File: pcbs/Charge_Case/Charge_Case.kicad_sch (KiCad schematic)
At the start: 3 parts, among them J1 GSB1C41110SSHR

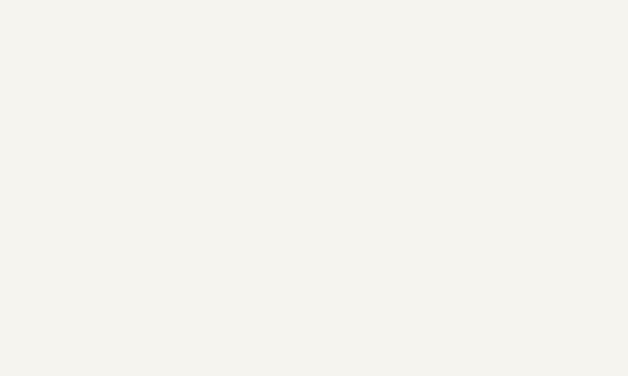
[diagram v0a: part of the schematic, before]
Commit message: update minibot fw, add pcb ordered packages
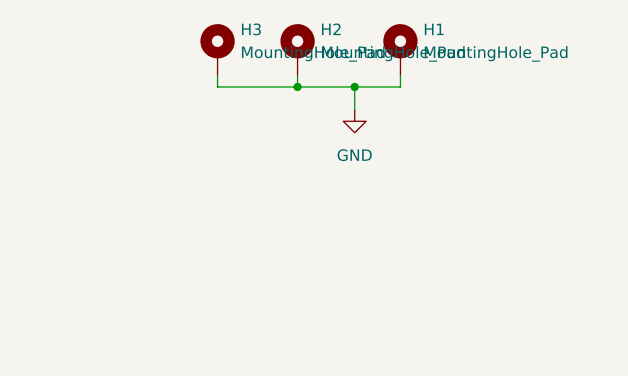
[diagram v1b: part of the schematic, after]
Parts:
- added H1, H2, H3: MountingHole_Pad, MountingHole:MountingHole_2.7mm_M2.5_DIN965_Pad_TopOnly, symbol Mechanical:MountingHole_Pad
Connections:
- net GND: now also H1.1, H2.1, H3.1
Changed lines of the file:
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@@
 (kicad_sch (version 20230121) (generator eeschema)
   (paper "A4")
+  (junction (at 242.57 35.56) (diameter 0) (color 0 0 0 0)
+  )
+  (junction (at 248.92 35.56) (diameter 0) (color 0 0 0 0)
+  )
   (no_connect (at 72.39 46.99))
   (no_connect (at 36.83 49.53))
@@
   (no_connect (at 72.39 49.53))
   (no_connect (at 72.39 54.61))
+  (wire (pts (xy 248.92 35.56) (xy 248.92 38.1))
+    (stroke (width 0) (type default))
+  )
   (wire (pts (xy 36.83 46.99) (xy 39.37 46.99))
     (stroke (width 0) (type default))
@@
     (stroke (width 0) (type default))
   )
+  (wire (pts (xy 233.68 35.56) (xy 242.57 35.56))
+    (stroke (width 0) (type default))
+  )
   (wire (pts (xy 69.85 49.53) (xy 72.39 49.53))
     (stroke (width 0) (type default))
@@
     (stroke (width 0) (type default))
   )
+  (wire (pts (xy 242.57 35.56) (xy 248.92 35.56))
+    (stroke (width 0) (type default))
+  )
+  (wire (pts (xy 242.57 34.29) (xy 242.57 35.56))
+    (stroke (width 0) (type default))
+  )
   (wire (pts (xy 31.75 36.83) (xy 39.37 36.83))
     (stroke (width 0) (type default))
@@
     (stroke (width 0) (type default))
   )
+  (wire (pts (xy 233.68 34.29) (xy 233.68 35.56))
+    (stroke (width 0) (type default))
+  )
   (wire (pts (xy 107.95 109.22) (xy 110.49 109.22))
     (stroke (width 0) (type default))
@@
     (stroke (width 0) (type default))
   )
+  (wire (pts (xy 254 35.56) (xy 248.92 35.56))
+    (stroke (width 0) (type default))
+  )
   (wire (pts (xy 36.83 44.45) (xy 36.83 46.99))
     (stroke (width 0) (type default))
@@
   )
   (wire (pts (xy 107.95 76.2) (xy 110.49 76.2))
+    (stroke (width 0) (type default))
+  )
+  (wire (pts (xy 254 34.29) (xy 254 35.56))
     (stroke (width 0) (type default))
   )
@@
   (label "CC2_SRC" (at 72.39 36.83 0) (fields_autoplaced)
     (effects (font (size 1.27 1.27)) (justify left bottom))
+  )
+  (symbol (lib_id "Mechanical:MountingHole_Pad") (at 254 31.75 0) (unit 1)
+    (in_bom yes) (on_board yes) (dnp no) (fields_autoplaced)
+    (property "Reference" "H1" (at 256.54 29.21 0)
+      (effects (font (size 1.27 1.27)) (justify left))
+    )
+    (property "Value" "MountingHole_Pad" (at 256.54 31.75 0)
+      (effects (font (size 1.27 1.27)) (justify left))
+    )
+    (property "Footprint" "MountingHole:MountingHole_2.7mm_M2.5_DIN965_Pad_TopOnly" (at 254 31.75 0)
+      (effects (font (size 1.27 1.27)) hide)
+    )
+    (property "Datasheet" "~" (at 254 31.75 0)
+      (effects (font (size 1.27 1.27)) hide)
+    )
+    (pin "1")
+    (instances
+      (project "Charge_Case"
+        (path "/c60e6ee3-9293-40aa-b626-5d3d0add00e1"
+          (reference "H1") (unit 1)
+        )
+      )
+    )
   )
   (symbol (lib_id "power:+5V") (at 31.75 52.07 90) (unit 1)
@@
     )
   )
+  (symbol (lib_id "Mechanical:MountingHole_Pad") (at 233.68 31.75 0) (unit 1)
+    (in_bom yes) (on_board yes) (dnp no) (fields_autoplaced)
+    (property "Reference" "H3" (at 236.22 29.21 0)
+      (effects (font (size 1.27 1.27)) (justify left))
+    )
+    (property "Value" "MountingHole_Pad" (at 236.22 31.75 0)
+      (effects (font (size 1.27 1.27)) (justify left))
+    )
+    (property "Footprint" "MountingHole:MountingHole_2.7mm_M2.5_DIN965_Pad_TopOnly" (at 233.68 31.75 0)
+      (effects (font (size 1.27 1.27)) hide)
+    )
+    (property "Datasheet" "~" (at 233.68 31.75 0)
+      (effects (font (size 1.27 1.27)) hide)
+    )
+    (pin "1")
+    (instances
+      (project "Charge_Case"
+        (path "/c60e6ee3-9293-40aa-b626-5d3d0add00e1"
+          (reference "H3") (unit 1)
+        )
+      )
+    )
+  )
   (symbol (lib_id "Jumper:Jumper_2_Bridged") (at 102.87 38.1 0) (unit 1)
     (in_bom yes) (on_board yes) (dnp no) (fields_autoplaced)
@@
     )
   )
+  (symbol (lib_id "Mechanical:MountingHole_Pad") (at 242.57 31.75 0) (unit 1)
+    (in_bom yes) (on_board yes) (dnp no) (fields_autoplaced)
+    (property "Reference" "H2" (at 245.11 29.21 0)
+      (effects (font (size 1.27 1.27)) (justify left))
+    )
+    (property "Value" "MountingHole_Pad" (at 245.11 31.75 0)
+      (effects (font (size 1.27 1.27)) (justify left))
+    )
+    (property "Footprint" "MountingHole:MountingHole_2.7mm_M2.5_DIN965_Pad_TopOnly" (at 242.57 31.75 0)
+      (effects (font (size 1.27 1.27)) hide)
+    )
+    (property "Datasheet" "~" (at 242.57 31.75 0)
+      (effects (font (size 1.27 1.27)) hide)
+    )
+    (pin "1")
+    (instances
+      (project "Charge_Case"
+        (path "/c60e6ee3-9293-40aa-b626-5d3d0add00e1"
+          (reference "H2") (unit 1)
+        )
+      )
+    )
+  )
   (symbol (lib_id "power:GND") (at 31.75 36.83 270) (unit 1)
     (in_bom yes) (on_board yes) (dnp no) (fields_autoplaced)
@@
         )
       )
+    )
+  )
+  (symbol (lib_id "power:GND") (at 248.92 38.1 0) (unit 1)
+    (in_bom yes) (on_board yes) (dnp no) (fields_autoplaced)
+    (property "Reference" "#PWR053" (at 248.92 44.45 0)
+      (effects (font (size 1.27 1.27)) hide)
+    )
+    (property "Value" "GND" (at 248.92 43.18 0)
+      (effects (font (size 1.27 1.27)))
+    )
+    (property "Footprint" "" (at 248.92 38.1 0)
+      (effects (font (size 1.27 1.27)) hide)
+    )
+    (property "Datasheet" "" (at 248.92 38.1 0)
+      (effects (font (size 1.27 1.27)) hide)
+    )
+    (pin "1")
+    (instances
+      (project "Charge_Case"
+        (path "/c60e6ee3-9293-40aa-b626-5d3d0add00e1"
+          (reference "#PWR053") (unit 1)
+        )
+      )
